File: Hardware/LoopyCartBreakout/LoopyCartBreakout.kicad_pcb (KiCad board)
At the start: 2 copper layers, 100 x 90 mm, 15 parts, among them J1 CONSOLE, J10 CON8, J11 CON9, J12 SOCKET, J2 PASSTHRU, J3 CON1, J4 CON2, J5 CON3, J6 CON4, J7 CON5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

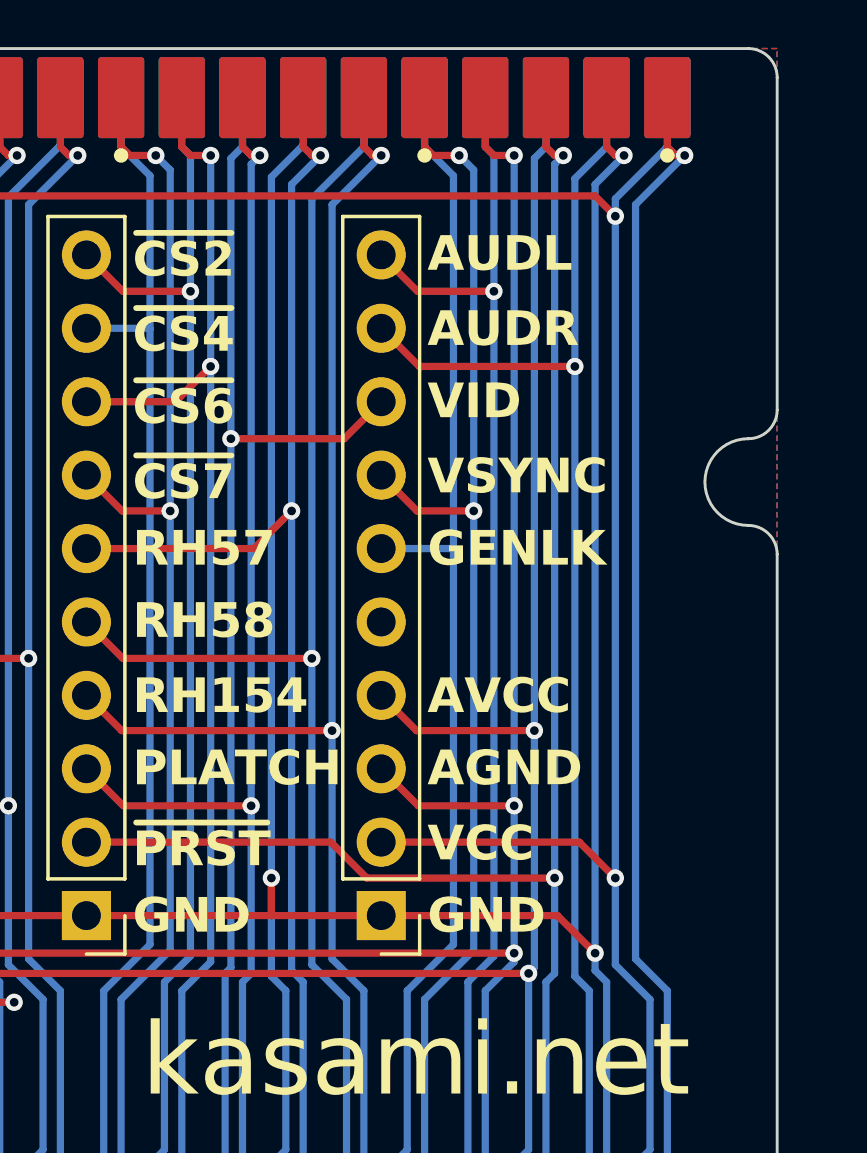
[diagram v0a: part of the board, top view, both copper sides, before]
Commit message: Fix breakout to separate VGND
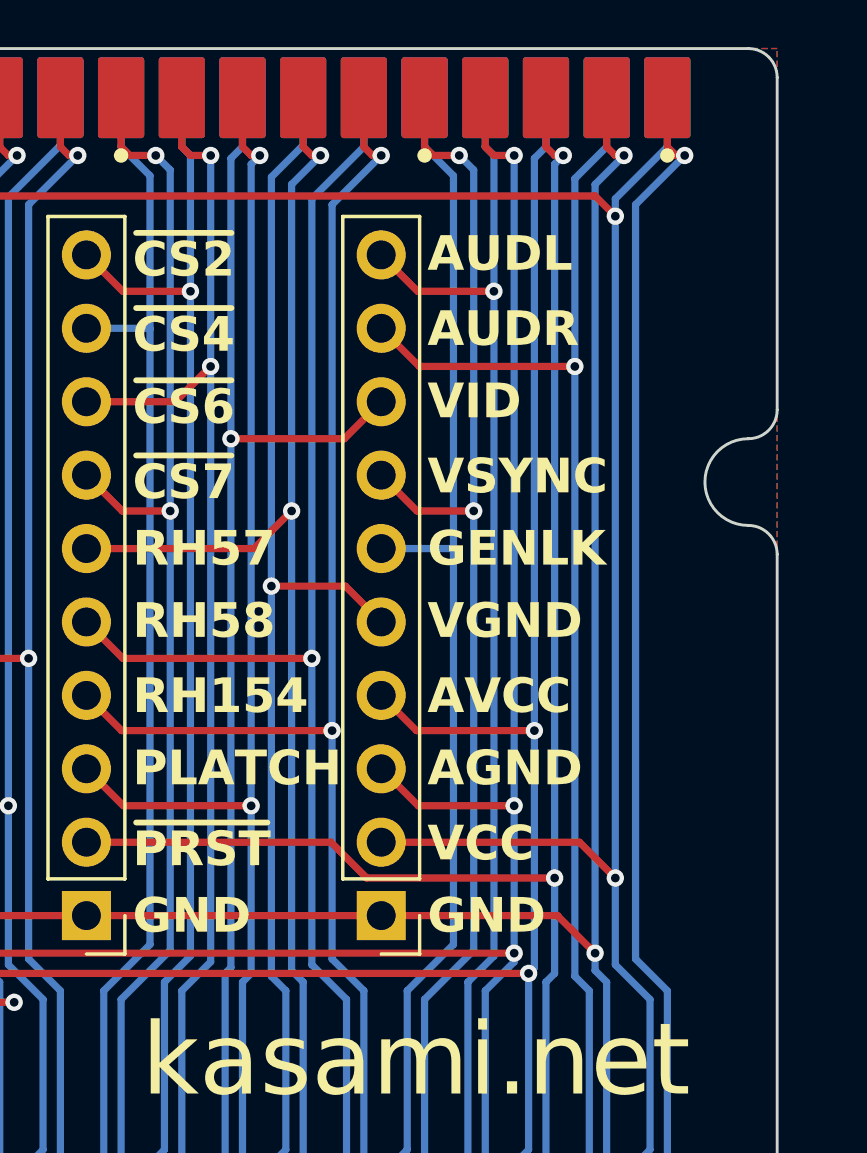
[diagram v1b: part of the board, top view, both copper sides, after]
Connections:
- J1 pad 7: /GND -> /VGND
- J11 pad 5: unconnected-(J11-Pin_5-Pad5) -> /VGND
- J12 pad 7: /GND -> /VGND
- J2 pad 7: /GND -> /VGND
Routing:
- net /VGND: track 0.00 -> 91.8 mm, vias 0 -> 1
- net /GND: track 536.1 -> 447.4 mm, vias 6 -> 5
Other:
- board text added: "VGND"
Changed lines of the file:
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@@
       (layer "B.Paste" (type "Bottom Solder Paste"))
       (layer "B.SilkS" (type "Bottom Silk Screen") (color "White"))
+      (copper_finish "None")
       (dielectric_constraints no)
     )
@@
   (net 81 "/D11")
   (net 82 "unconnected-(J7-Pin_2-Pad2)")
-  (net 83 "unconnected-(J11-Pin_5-Pad5)")
+  (net 83 "/VGND")
   (footprint "Connector_PinHeader_2.54mm:PinHeader_1x10_P2.54mm_Vertical" (layer "F.Cu")
     (at 163.8 88 180)
@@
       (net 3 "/AVCC") (pinfunction "Pin_4") (pintype "passive"))
     (pad "5" thru_hole oval (at 0 10.16 180) (size 1.7 1.7) (drill 1) (layers "*.Cu" "*.Mask")
-      (net 83 "unconnected-(J11-Pin_5-Pad5)") (pinfunction "Pin_5") (pintype "passive+no_connect"))
+      (net 83 "/VGND") (pinfunction "Pin_5") (pintype "passive"))
     (pad "6" thru_hole oval (at 0 12.7 180) (size 1.7 1.7) (drill 1) (layers "*.Cu" "*.Mask")
       (net 5 "/GENLK") (pinfunction "Pin_6") (pintype "passive"))
@@
       ))
     (pad "7" connect custom (at 33.6 1.8) (size 1 1) (layers "B.Cu" "B.Mask")
-      (net 7 "/GND") (pinfunction "GND") (pintype "passive") (thermal_bridge_angle 45)
+      (net 83 "/VGND") (pinfunction "GND") (pintype "passive") (thermal_bridge_angle 45)
       (options (clearance outline) (anchor rect))
       (primitives
@@
       (net 6 "/RH58") (pinfunction "RH58?") (pintype "bidirectional") (thermal_bridge_angle 45))
     (pad "7" smd roundrect (at 33.6 0) (size 1.6 2.8) (layers "B.Cu" "B.Mask") (roundrect_rratio 0.0625)
-      (net 7 "/GND") (pinfunction "GND") (pintype "power_in") (thermal_bridge_angle 45))
+      (net 83 "/VGND") (pinfunction "GND") (pintype "power_in") (thermal_bridge_angle 45))
     (pad "8" smd roundrect (at 31.5 0) (size 1.6 2.8) (layers "B.Cu" "B.Mask") (roundrect_rratio 0.0625)
       (net 8 "/VID") (pinfunction "VID") (pintype "output") (thermal_bridge_angle 45))
@@
       (net 6 "/RH58") (pinfunction "RH58?") (pintype "bidirectional") (thermal_bridge_angle 45))
     (pad "7" thru_hole oval (at 33.6 1.5) (size 2 2) (drill 1) (layers "*.Cu" "*.Mask")
-      (net 7 "/GND") (pinfunction "GND") (pintype "power_in") (thermal_bridge_angle 45))
+      (net 83 "/VGND") (pinfunction "GND") (pintype "power_in") (thermal_bridge_angle 45))
     (pad "8" thru_hole oval (at 31.5 4.5) (size 2 2) (drill 1) (layers "*.Cu" "*.Mask")
       (net 8 "/VID") (pinfunction "VID") (pintype "output") (thermal_bridge_angle 45))
@@
     (effects (font (size 1.2 1.2) (thickness 0.2) bold) (justify left mirror))
   )
+  (gr_text "VGND" (at 195.9 77.8) (layer "B.SilkS")
+    (effects (font (size 1.2 1.2) (thickness 0.2) bold) (justify right mirror))
+  )
   (gr_text "D14" (at 114.6 67.7) (layer "B.SilkS")
     (effects (font (size 1.2 1.2) (thickness 0.2) bold) (justify right mirror))
@@
     (effects (font (size 1.2 1.2) (thickness 0.2) bold) (justify right mirror))
   )
-  (gr_text "GND" (at 191.6 138 -90) (layer "B.SilkS")
+  (gr_text "VGND" (at 191.6 138 270) (layer "B.SilkS")
     (effects (font (size 1.2 1.2) (thickness 0.2) bold) (justify left mirror))
   )
@@
     (effects (font (size 1.2 1.2) (thickness 0.2) bold) (justify left))
   )
+  (gr_text "VGND" (at 195.9 77.8) (layer "F.SilkS")
+    (effects (font (size 1.2 1.2) (thickness 0.2) bold) (justify left))
+  )
   (gr_text "A5" (at 155.2 65.1) (layer "F.SilkS")
     (effects (font (size 1.2 1.2) (thickness 0.2) bold) (justify left))
@@
   (segment (start 202.4 61.7) (end 202.1 61.4) (width 0.25) (layer "F.Cu") (net 7))
   (segment (start 202.1 108.5) (end 202.1 145.6) (width 0.25) (layer "F.Cu") (net 7))
-  (segment (start 190.5 86.7) (end 190.5 88) (width 0.25) (layer "F.Cu") (net 7))
   (segment (start 200.7 107.1) (end 202.1 108.5) (width 0.25) (layer "F.Cu") (net 7))
   (segment (start 190.5 88) (end 194.3 88) (width 0.25) (layer "F.Cu") (net 7))
@@
   (segment (start 143.6 61.7) (end 143.3 61.4) (width 0.25) (layer "F.Cu") (net 7))
   (segment (start 202.7 61.7) (end 202.4 61.7) (width 0.25) (layer "F.Cu") (net 7))
-  (via (at 190.5 86.7) (size 0.6) (drill 0.3) (layers "F.Cu" "B.Cu") (net 7))
   (via (at 178.6 86.7) (size 0.6) (drill 0.3) (layers "F.Cu" "B.Cu") (net 7))
   (via (at 202.7 61.7) (size 0.6) (drill 0.3) (layers "F.Cu" "B.Cu") (net 7))
@@
   (segment (start 178.4 96.1) (end 177.6 96.9) (width 0.25) (layer "B.Cu") (net 7))
   (segment (start 178.4 90) (end 178.4 96.1) (width 0.25) (layer "B.Cu") (net 7))
-  (segment (start 190.5 62.445405) (end 190.5 86.7) (width 0.25) (layer "B.Cu") (net 7))
-  (segment (start 190.5 86.7) (end 190.5 90.1) (width 0.25) (layer "B.Cu") (net 7))
   (segment (start 146.4 88) (end 146.4 63.6) (width 0.25) (layer "B.Cu") (net 7))
   (segment (start 143.3 92.3) (end 146.4 89.2) (width 0.25) (layer "B.Cu") (net 7))
@@
   (segment (start 111.2 96.1) (end 111.2 92) (width 0.25) (layer "B.Cu") (net 7))
   (segment (start 114.2 89) (end 114.2 88) (width 0.25) (layer "B.Cu") (net 7))
-  (segment (start 191 96.1) (end 190.2 96.9) (width 0.25) (layer "B.Cu") (net 7))
-  (segment (start 190.2 96.9) (end 190.2 98.6) (width 0.25) (layer "B.Cu") (net 7))
   (segment (start 202.1 100.5) (end 202.1 90.3) (width 0.25) (layer "B.Cu") (net 7))
   (segment (start 178.6 61.745405) (end 178.6 86.7) (width 0.25) (layer "B.Cu") (net 7))
@@
   (segment (start 110.4 98.6) (end 110.4 96.9) (width 0.25) (layer "B.Cu") (net 7))
   (segment (start 110.4 96.9) (end 111.2 96.1) (width 0.25) (layer "B.Cu") (net 7))
-  (segment (start 191.6 59.7) (end 191.6 61.345405) (width 0.25) (layer "B.Cu") (net 7))
   (segment (start 146.4 89.2) (end 146.4 88) (width 0.25) (layer "B.Cu") (net 7))
   (segment (start 179 100) (end 179 103.5) (width 0.25) (layer "B.Cu") (net 7))
-  (segment (start 191.6 100) (end 191.6 103.5) (width 0.25) (layer "B.Cu") (net 7))
   (segment (start 201.7 89.9) (end 201.7 62.7) (width 0.25) (layer "B.Cu") (net 7))
   (segment (start 114.2 88) (end 114.2 63.8) (width 0.25) (layer "B.Cu") (net 7))
@@
   (segment (start 111.2 92) (end 114.2 89) (width 0.25) (layer "B.Cu") (net 7))
   (segment (start 201.7 62.7) (end 202.7 61.7) (width 0.25) (layer "B.Cu") (net 7))
-  (segment (start 190.5 90.1) (end 191 90.6) (width 0.25) (layer "B.Cu") (net 7))
   (segment (start 179 59.7) (end 179 61.345405) (width 0.25) (layer "B.Cu") (net 7))
   (segment (start 111.8 61.4) (end 111.8 59.7) (width 0.25) (layer "B.Cu") (net 7))
   (segment (start 179 61.345405) (end 178.6 61.745405) (width 0.25) (layer "B.Cu") (net 7))
-  (segment (start 191.6 145.6) (end 191.6 103.5) (width 0.25) (layer "B.Cu") (net 7))
-  (segment (start 190.2 98.6) (end 191.6 100) (width 0.25) (layer "B.Cu") (net 7))
   (segment (start 177.6 98.6) (end 179 100) (width 0.25) (layer "B.Cu") (net 7))
   (segment (start 202.1 90.3) (end 201.7 89.9) (width 0.25) (layer "B.Cu") (net 7))
   (segment (start 178.6 86.7) (end 178.6 89.8) (width 0.25) (layer "B.Cu") (net 7))
-  (segment (start 191 90.6) (end 191 96.1) (width 0.25) (layer "B.Cu") (net 7))
-  (segment (start 191.6 61.345405) (end 190.5 62.445405) (width 0.25) (layer "B.Cu") (net 7))
   (segment (start 193.02 71.5) (end 189.1 71.5) (width 0.25) (layer "F.Cu") (net 8))
   (segment (start 194.3 70.22) (end 193.02 71.5) (width 0.25) (layer "F.Cu") (net 8))
@@
   (segment (start 114.9 89.2) (end 111.8 92.3) (width 0.25) (layer "B.Cu") (net 81))
   (segment (start 114.9 76.6) (end 114.9 63.6) (width 0.25) (layer "B.Cu") (net 81))
+  (segment (start 194.3 77.84) (end 193.06 76.6) (width 0.25) (layer "F.Cu") (net 83))
+  (segment (start 193.06 76.6) (end 190.5 76.6) (width 0.25) (layer "F.Cu") (net 83))
+  (via (at 190.5 76.6) (size 0.6) (drill 0.3) (layers "F.Cu" "B.Cu") (net 83))
+  (segment (start 190.5 76.6) (end 190.5 90.1) (width 0.25) (layer "B.Cu") (net 83))
+  (segment (start 190.2 98.6) (end 191.6 100) (width 0.25) (layer "B.Cu") (net 83))
+  (segment (start 190.2 96.9) (end 190.2 98.6) (width 0.25) (layer "B.Cu") (net 83))
+  (segment (start 190.5 62.445405) (end 190.5 76.6) (width 0.25) (layer "B.Cu") (net 83))
+  (segment (start 191.6 100) (end 191.6 103.5) (width 0.25) (layer "B.Cu") (net 83))
+  (segment (start 191.6 59.7) (end 191.6 61.345405) (width 0.25) (layer "B.Cu") (net 83))
+  (segment (start 191 96.1) (end 190.2 96.9) (width 0.25) (layer "B.Cu") (net 83))
+  (segment (start 191.6 61.345405) (end 190.5 62.445405) (width 0.25) (layer "B.Cu") (net 83))
+  (segment (start 191 90.6) (end 191 96.1) (width 0.25) (layer "B.Cu") (net 83))
+  (segment (start 190.5 90.1) (end 191 90.6) (width 0.25) (layer "B.Cu") (net 83))
+  (segment (start 191.6 145.6) (end 191.6 103.5) (width 0.25) (layer "B.Cu") (net 83))
   (zone (net 0) (net_name "") (layers "F&B.Cu") (hatch edge 0.5)
     (connect_pads (clearance 0.25))

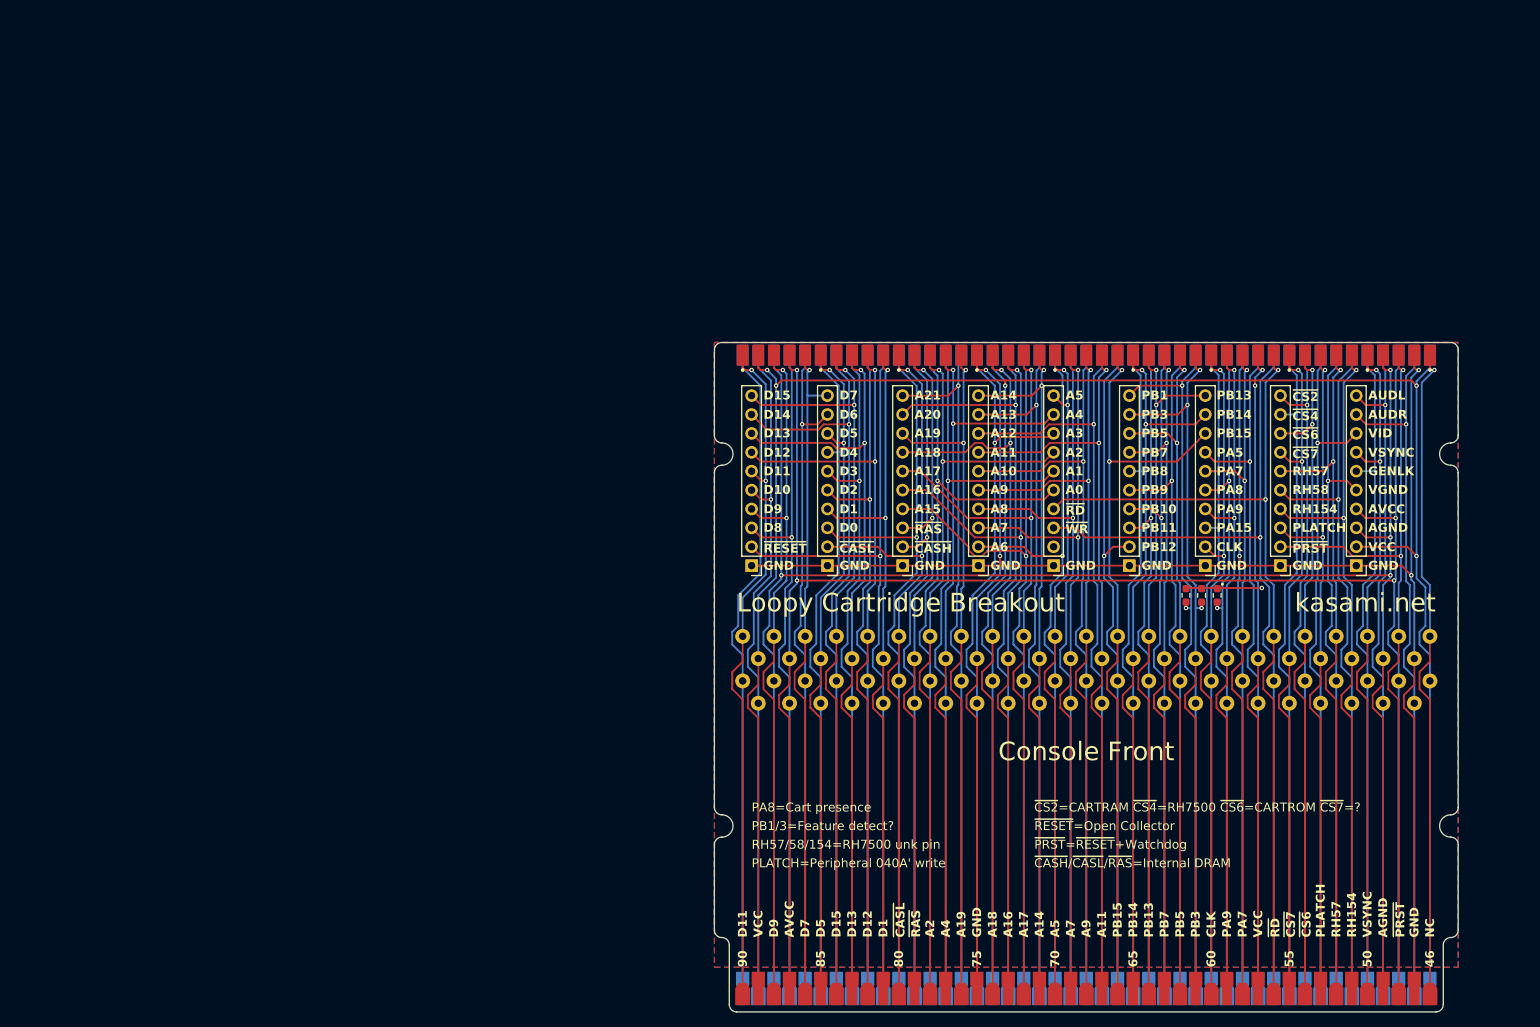
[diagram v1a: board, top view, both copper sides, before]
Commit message: Update cart breakout board & treat kicad files as binary
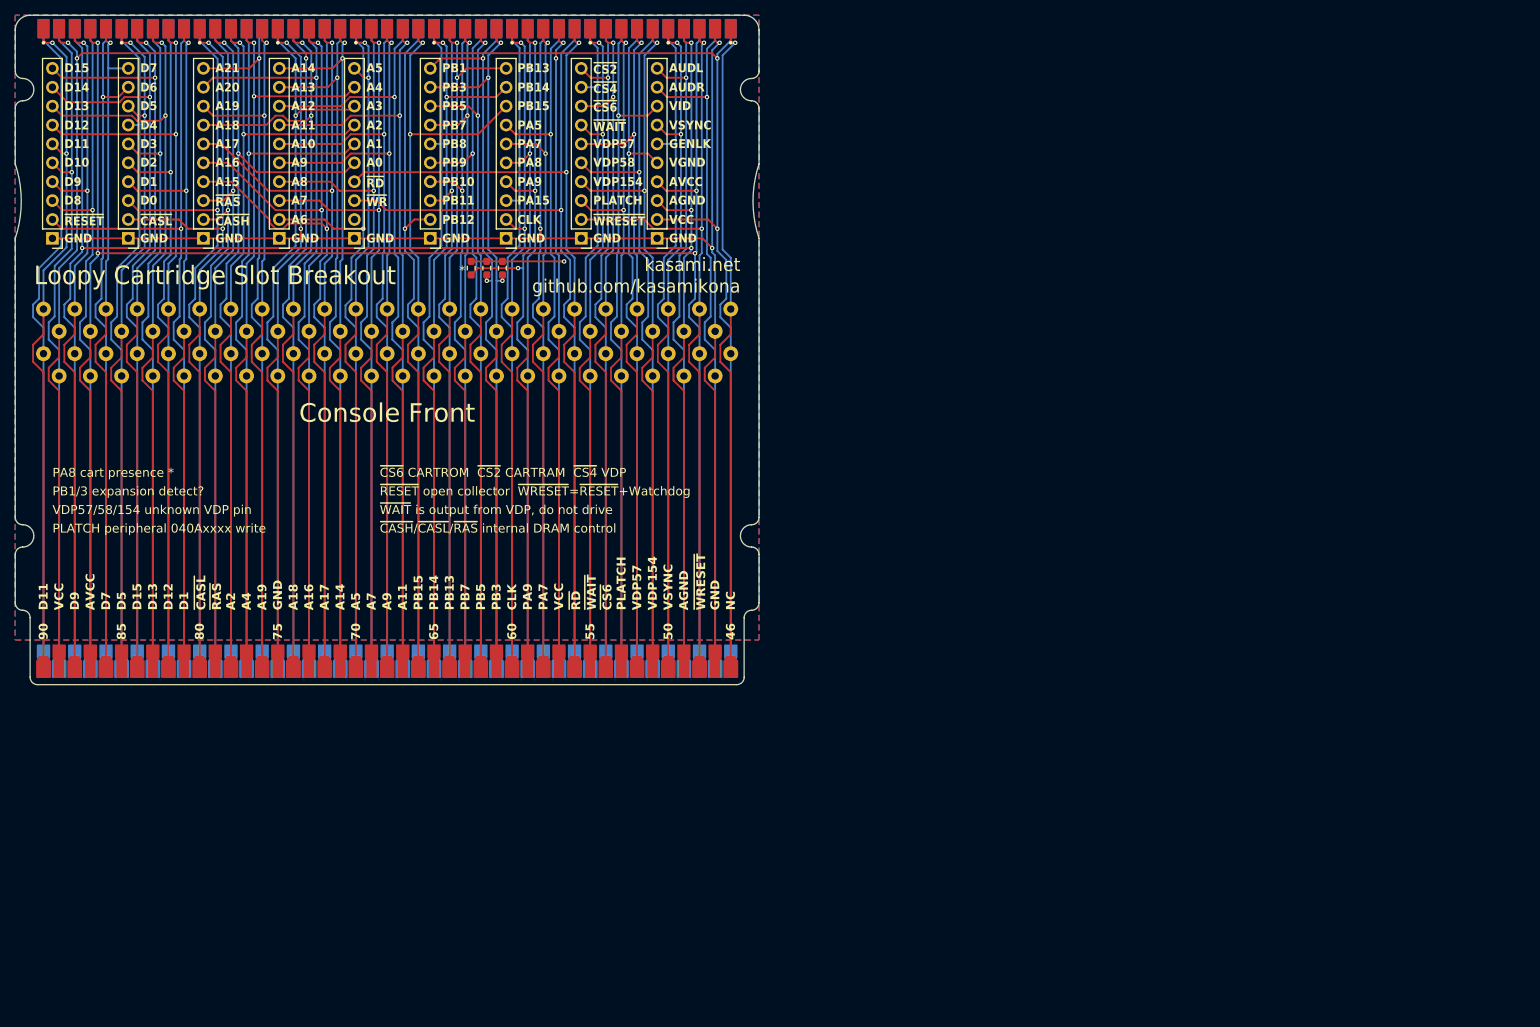
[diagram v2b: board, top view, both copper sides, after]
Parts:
- moved R1 109.5 mm to (75.3, 48.0)
- moved J11 103.8 mm to (100.3, 44.0)
- moved J5 103.8 mm to (39.3, 44.0)
- moved J8 103.8 mm to (69.8, 44.0)
- moved J1 103.8 mm to (64.0, 99.8)
- moved J10 103.8 mm to (90.1, 44.0)
- moved J12 103.8 mm to (64.0, 58.0)
- moved J2 103.8 mm to (64.0, 15.7)
- moved J3 103.8 mm to (19.0, 44.0)
- moved J4 103.8 mm to (29.2, 44.0)
- moved J6 103.8 mm to (49.5, 44.0)
- moved J7 103.8 mm to (59.6, 44.0)
- moved J9 103.8 mm to (80.0, 44.0)
- moved R2 103.8 mm to (77.4, 48.0)
- moved R3 103.8 mm to (79.5, 48.0)
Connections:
- net /CS7 renamed /WAIT
- net /PRST renamed /WRESET
- net /RH154 renamed /VDP154
- net /RH57 renamed /VDP57
- net /RH58 renamed /VDP58
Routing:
- net /PA8: track 92.5 -> 98.4 mm
- net /VCC: track 461.7 -> 464.1 mm
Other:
- outline, holes or cut-outs redrawn
- board text added: "*"
- board text added: "Loopy Cartridge Slot Breakout"
- board text added: "PA8 cart presence *"
- board text added: "PB1/3 expansion detect?"
- board text added: "PLATCH peripheral 040Axxxx write"
- board text added: "VDP154"
- board text added: "VDP57"
- board text added: "VDP57/58/154 unknown VDP pin"
- board text added: "VDP58"
- board text added: "kasami.net github.com/kasamikona"
- board text added: "~{CASH}/~{CASL}/~{RAS} internal DRAM control"
- board text added: "~{CS6} CARTROM ~{CS2} CARTRAM ~{CS4} VDP"
- board text added: "~{RESET} open collector ~{WRESET}=~{RESET}+Watchdog"
- board text added: "~{WAIT}"
- board text added: "~{WAIT} is output from VDP, do not drive"
- board text added: "~{WRESET}"
- board text removed: "21"
- board text removed: "Loopy Cartridge Breakout"
- board text removed: "PA8=Cart presence"
- board text removed: "PB1/3=Feature detect?"
- board text removed: "PLATCH=Peripheral 040A' write"
- board text removed: "Passthrough for prototype cart - solder here if you're brave enough"
- board text removed: "RH154"
- board text removed: "RH57"
- board text removed: "RH57/58/154=RH7500 unk pin"
- board text removed: "RH58"
- board text removed: "kasami.net"
- board text removed: "~{CASH}/~{CASL}/~{RAS}=Internal DRAM"
- board text removed: "~{CS2}=CARTRAM ~{CS4}=RH7500 ~{CS6}=CARTROM ~{CS7}=?"
- board text removed: "~{PRST}"
- board text removed: "~{PRST}=~{RESET}+Watchdog"
- board text removed: "~{RESET}=Open Collector"
